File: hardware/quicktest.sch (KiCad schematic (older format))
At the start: 49 parts

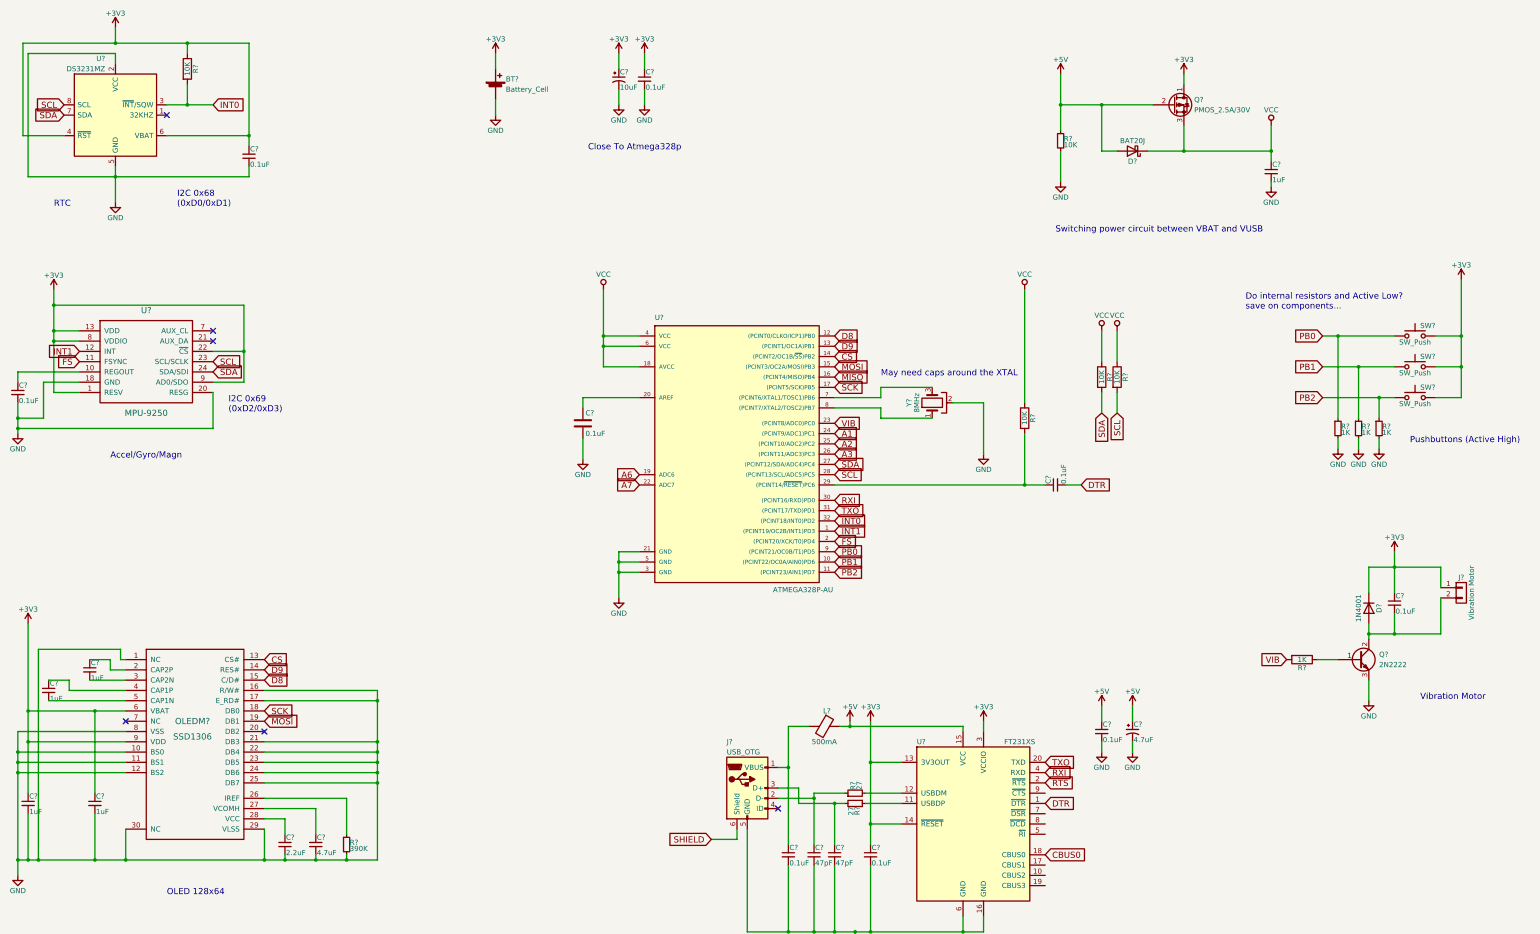
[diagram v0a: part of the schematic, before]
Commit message: added annotations
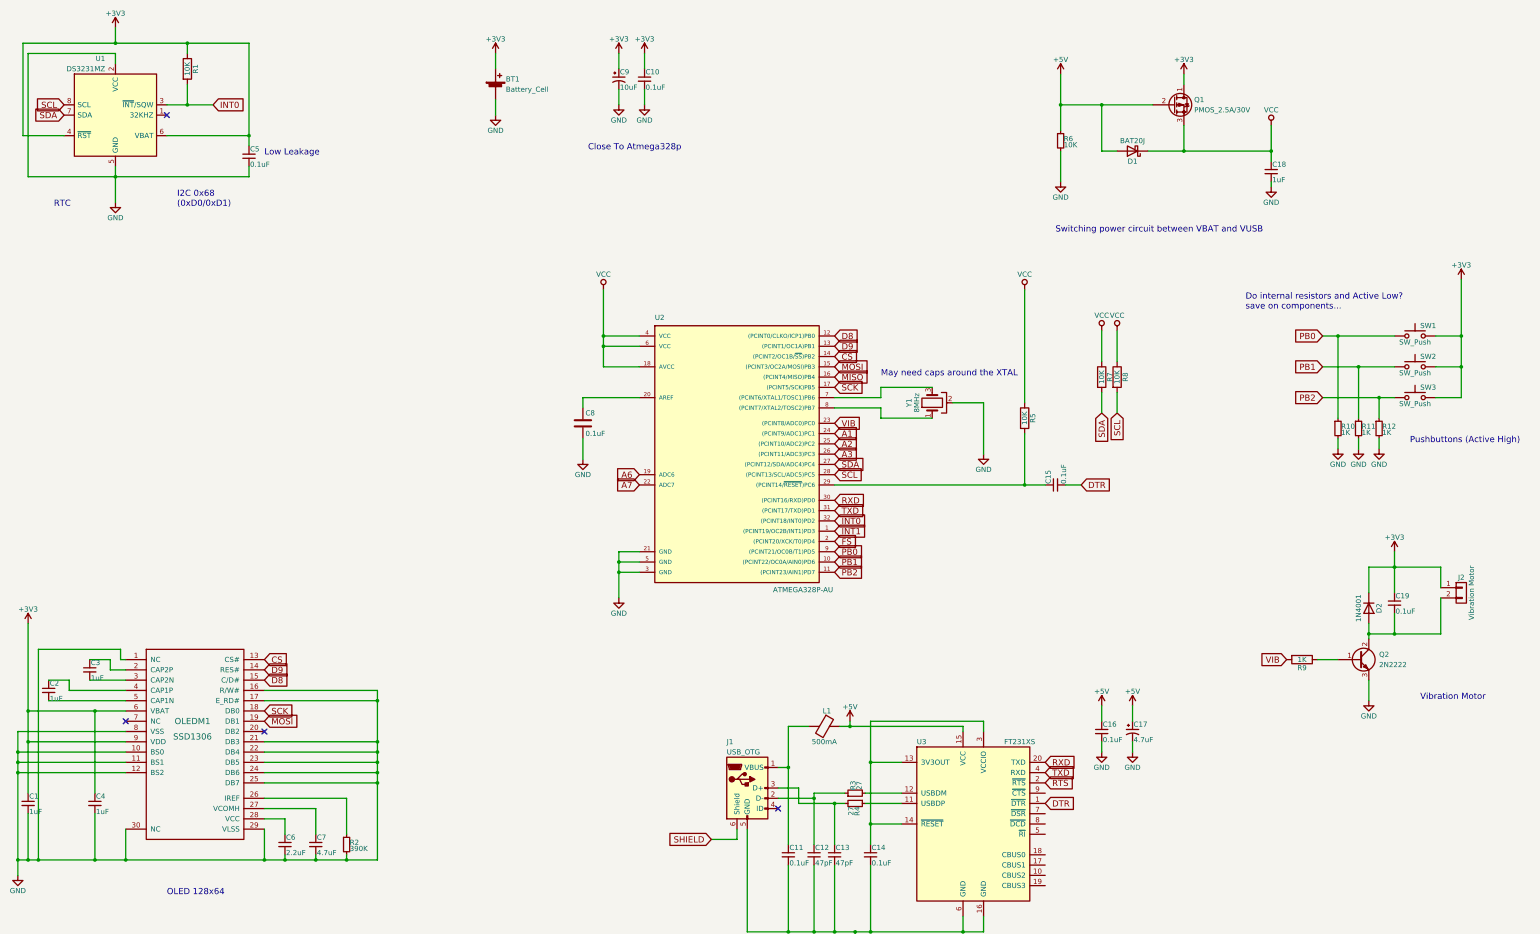
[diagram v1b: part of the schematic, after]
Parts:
- removed C?: 0.1uF, symbol C_Small
- removed U?: MPU-9250, symbol MPU-9250
- gave numbers to parts that had none: 47
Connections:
- net +3V3: no longer C14.1, U3.13 (3V3OUT), U3.14 (~RESET), U3.3 (VCCIO)
- net CBUS0: no longer names the net of U3.18 (CBUS0)
- net RXI renamed RXD
- net RXD: now also U3.20 (TXD); no longer U3.4 (RXD)
- net TXO renamed TXD
- net TXD: now also U3.4 (RXD); no longer U3.20 (TXD)
- new net: C14.1, U3.13 (3V3OUT), U3.14 (~RESET), U3.3 (VCCIO)
- no-connect marks 6 -> 4
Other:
- note added: "Low Leakage"
- note removed: "Accel/Gyro/Magn"
- note removed: "I2C 0x69\n(0xD2/0xD3)"

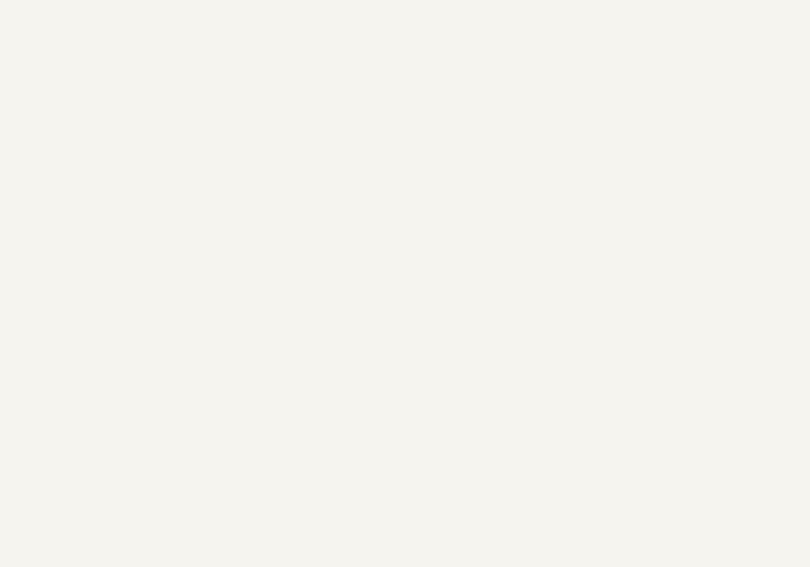
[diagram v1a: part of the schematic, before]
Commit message: added a ICSP connector for programming
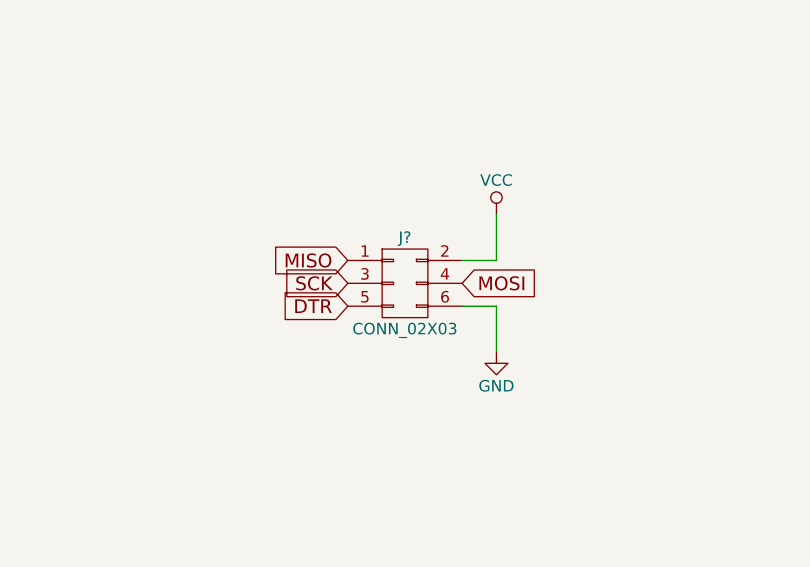
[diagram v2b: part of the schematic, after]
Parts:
- added J?: CONN_02X03, symbol CONN_02X03
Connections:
- net DTR: now also J?.5 (P5)
- net GND: now also J?.6 (P6)
- net MISO: now also J?.1 (P1)
- net MOSI: now also J?.4 (P4)
- net SCK: now also J?.3 (P3)
- net VCC: now also J?.2 (P2)
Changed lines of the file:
@@
 Wire Wire Line
 	10200 7600 9100 7600
+$Comp
+L CONN_02X03 J?
+U 1 1 5986D8F5
+P 3900 4800
+F 0 "J?" H 3900 5000 50  0000 C CNN
+F 1 "CONN_02X03" H 3900 4600 50  0000 C CNN
+F 2 "" H 3900 3600 50  0001 C CNN
+F 3 "" H 3900 3600 50  0001 C CNN
+	1    3900 4800
+	1    0    0    -1
+$EndComp
+Text GLabel 3650 4700 0    60   Input ~ 0
+MISO
+Text GLabel 3650 4800 0    60   Input ~ 0
+SCK
+Text GLabel 3650 4900 0    60   Input ~ 0
+DTR
+Text GLabel 4150 4800 2    60   Input ~ 0
+MOSI
+$Comp
+L VCC #PWR?
+U 1 1 5986F5F4
+P 4300 4500
+F 0 "#PWR?" H 4300 4350 50  0001 C CNN
+F 1 "VCC" H 4300 4650 50  0000 C CNN
+F 2 "" H 4300 4500 50  0001 C CNN
+F 3 "" H 4300 4500 50  0001 C CNN
+	1    4300 4500
+	1    0    0    -1
+$EndComp
+$Comp
+L GND #PWR?
+U 1 1 5986F668
+P 4300 5100
+F 0 "#PWR?" H 4300 4850 50  0001 C CNN
+F 1 "GND" H 4300 4950 50  0000 C CNN
+F 2 "" H 4300 5100 50  0001 C CNN
+F 3 "" H 4300 5100 50  0001 C CNN
+	1    4300 5100
+	1    0    0    -1
+$EndComp
+Wire Wire Line
+	4150 4900 4300 4900
+Wire Wire Line
+	4300 4900 4300 5100
+Wire Wire Line
+	4300 4500 4300 4700
+Wire Wire Line
+	4300 4700 4150 4700
 $EndSCHEMATC

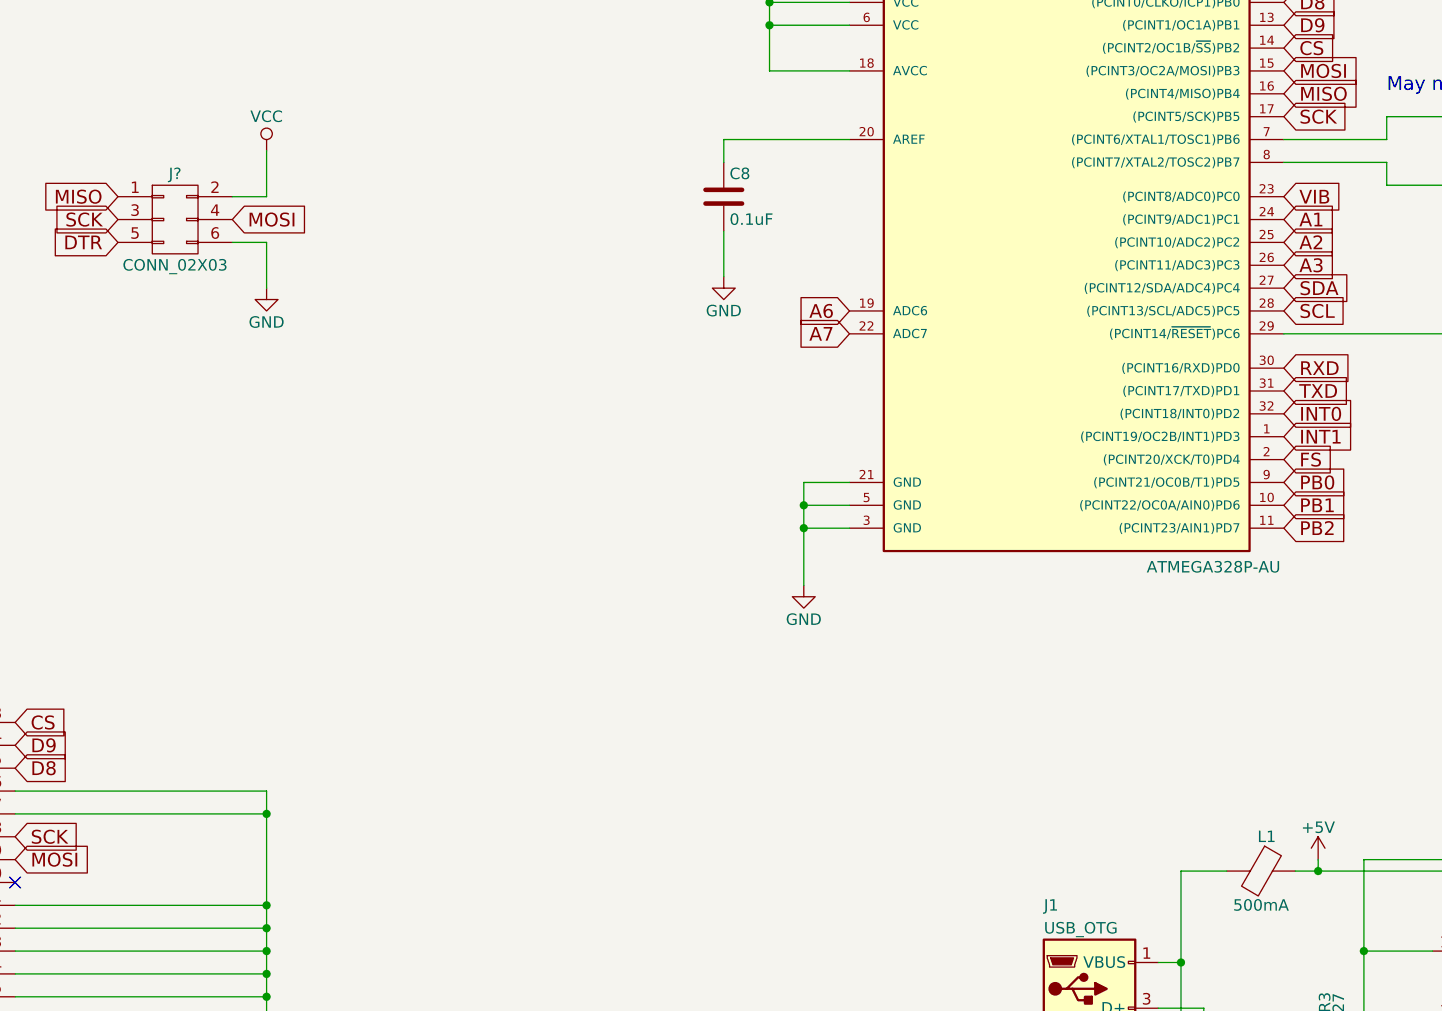
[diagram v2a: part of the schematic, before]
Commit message: choosing more footprints for components
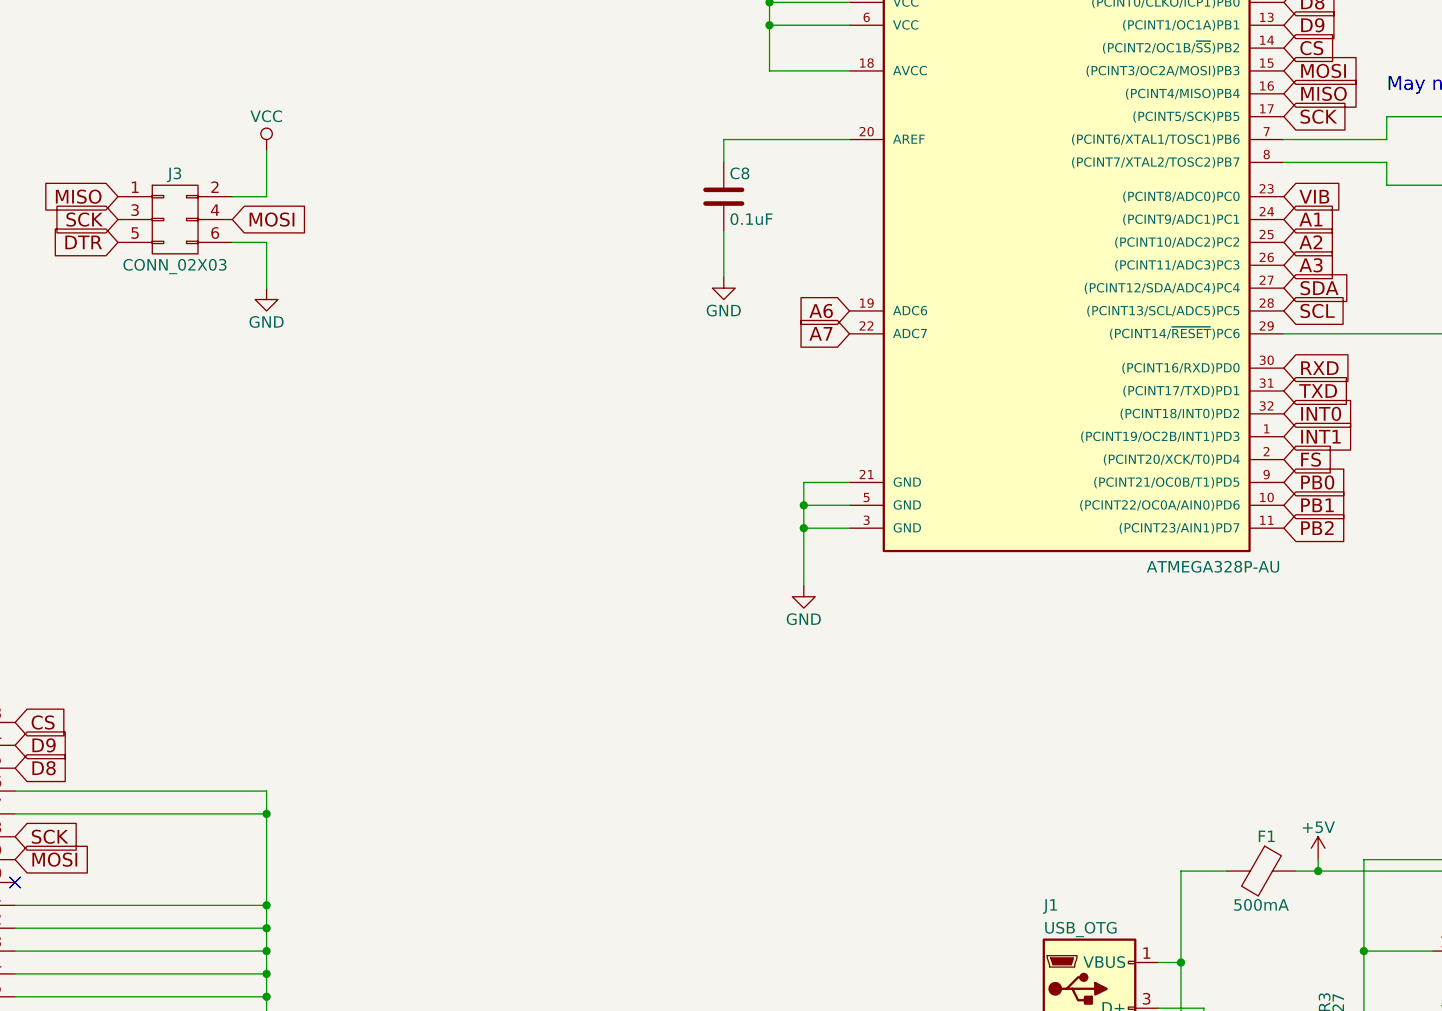
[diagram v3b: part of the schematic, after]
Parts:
- C1, C10, C11, C12, C13, C14, C15, C16, C18, C19, C2, C3, C4, C5, C6, C7, C8: footprint (none) -> Capacitors_SMD:C_0805
- C17, C9: footprint (none) -> Capacitors_THT:CP_Axial_L10.0mm_D4.5mm_P15.00mm_Horizontal
- D1: footprint (none) -> Diodes_SMD:D_SOD-323
- D2: footprint (none) -> Diodes_THT:D_DO-41_SOD81_P10.16mm_Horizontal
- F1: renamed from L1; footprint (none) -> Inductors_SMD:L_0603
- J1: footprint (none) -> Connectors:USB_Micro-B_10103594-0001LF
- J3: renamed from J?; footprint (none) -> Pin_Headers:Pin_Header_Straight_2x03_Pitch2.54mm
- R1, R10, R11, R12, R2, R3, R4, R5, R6, R7, R8, R9: footprint (none) -> Resistors_SMD:R_0805
- SW1, SW2, SW3: footprint (none) -> Buttons_Switches_SMD:SW_SPST_B3U-3000P
- U2: footprint TQFP32 -> Housings_QFP:TQFP-32_7x7mm_Pitch0.8mm
- U3: footprint SSOP-20 -> SMD_Packages:SSOP-20
- Y1: footprint (none) -> Crystals:Crystal_SMD_SeikoEpson_MA506-4pin_12.7x5.1mm

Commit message: doing some pcb work...also making a prototype case in scad
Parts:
- BT1: footprint (none) -> aw-1:Battery_Holder_SMT_LP2032SM-JJ-GTR
- C17, C9: footprint Capacitors_THT:CP_Axial_L10.0mm_D4.5mm_P15.00mm_Horizontal -> Capacitors_Tantalum_SMD:CP_Tantalum_Case-A_EIA-3216-18_Hand
- J2: footprint (none) -> Pin_Headers:Pin_Header_Straight_1x02_Pitch2.54mm
- OLEDM1: footprint (none) -> aw-1:SSD1306-FPC
- Q1: footprint (none) -> TO_SOT_Packages_SMD:SOT-23
- Q2: footprint (none) -> TO_SOT_Packages_THT:TO-18-3
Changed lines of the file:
@@
 F 0 "C9" H 6660 1420 50  0000 L CNN
 F 1 "10uF" H 6660 1270 50  0000 L CNN
-F 2 "Capacitors_THT:CP_Axial_L10.0mm_D4.5mm_P15.00mm_Horizontal" H 6650 1350 50  0001 C CNN
+F 2 "Capacitors_Tantalum_SMD:CP_Tantalum_Case-A_EIA-3216-18_Hand" H 6650 1350 50  0001 C CNN
 F 3 "" H 6650 1350 50  0001 C CNN
 	1    6650 1350
@@
 F 0 "J2" H 14850 6500 50  0000 C CNN
 F 1 "Vibration Motor" V 14950 6350 50  0000 C CNN
-F 2 "" H 14850 6350 50  0001 C CNN
+F 2 "Pin_Headers:Pin_Header_Straight_1x02_Pitch2.54mm" H 14850 6350 50  0001 C CNN
 F 3 "" H 14850 6350 50  0001 C CNN
 	1    14850 6350
@@
 F 0 "BT1" H 5550 1550 50  0000 L CNN
 F 1 "Battery_Cell" H 5550 1450 50  0000 L CNN
-F 2 "" V 5450 1510 50  0001 C CNN
+F 2 "aw-1:Battery_Holder_SMT_LP2032SM-JJ-GTR" V 5450 1510 50  0001 C CNN
 F 3 "" V 5450 1510 50  0001 C CNN
 	1    5450 1450
@@
 F 0 "Q2" H 14050 7050 50  0000 L CNN
 F 1 "2N2222" H 14050 6950 50  0000 L CNN
-F 2 "" H 14050 7100 50  0001 C CNN
+F 2 "TO_SOT_Packages_THT:TO-18-3" H 14050 7100 50  0001 C CNN
 F 3 "" H 13850 7000 50  0001 C CNN
 	1    13850 7000
@@
 F 0 "OLEDM1" H 2500 7900 60  0000 C CNN
 F 1 "SSD1306" H 2500 7750 60  0000 C CNN
-F 2 "" H 2600 7750 60  0001 C CNN
+F 2 "aw-1:SSD1306-FPC" H 2600 7750 60  0001 C CNN
 F 3 "" H 2600 7750 60  0000 C CNN
 	1    2600 7750
@@
 F 0 "C17" H 11660 7770 50  0000 L CNN
 F 1 "4.7uF" H 11660 7620 50  0000 L CNN
-F 2 "Capacitors_THT:CP_Axial_L10.0mm_D4.5mm_P15.00mm_Horizontal" H 11650 7700 50  0001 C CNN
+F 2 "Capacitors_Tantalum_SMD:CP_Tantalum_Case-A_EIA-3216-18_Hand" H 11650 7700 50  0001 C CNN
 F 3 "" H 11650 7700 50  0001 C CNN
 	1    11650 7700
@@
 F 0 "Q1" H 12250 1650 50  0000 L CNN
 F 1 "PMOS_2.5A/30V" H 12250 1550 50  0000 L CNN
-F 2 "" H 12250 1700 50  0001 C CNN
+F 2 "TO_SOT_Packages_SMD:SOT-23" H 12250 1700 50  0001 C CNN
 F 3 "" H 12050 1600 50  0001 C CNN
 	1    12050 1600
